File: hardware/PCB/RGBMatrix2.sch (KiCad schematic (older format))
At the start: 27 parts

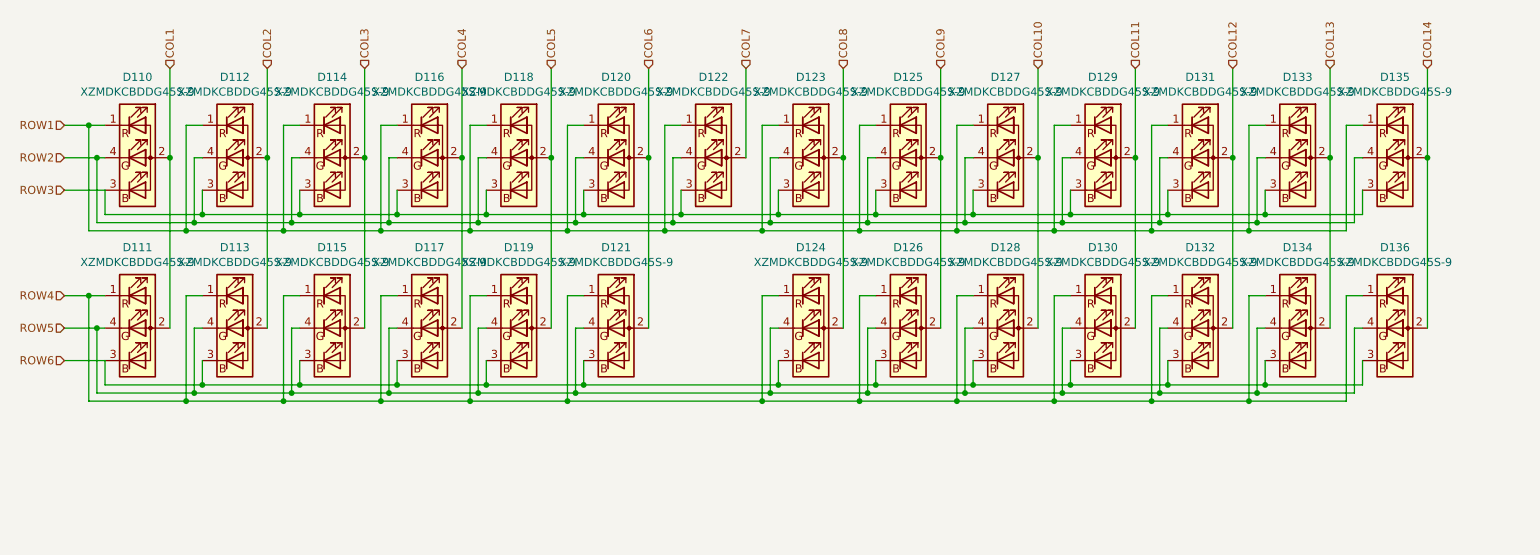
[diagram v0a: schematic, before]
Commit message: small improvements (cap distance)
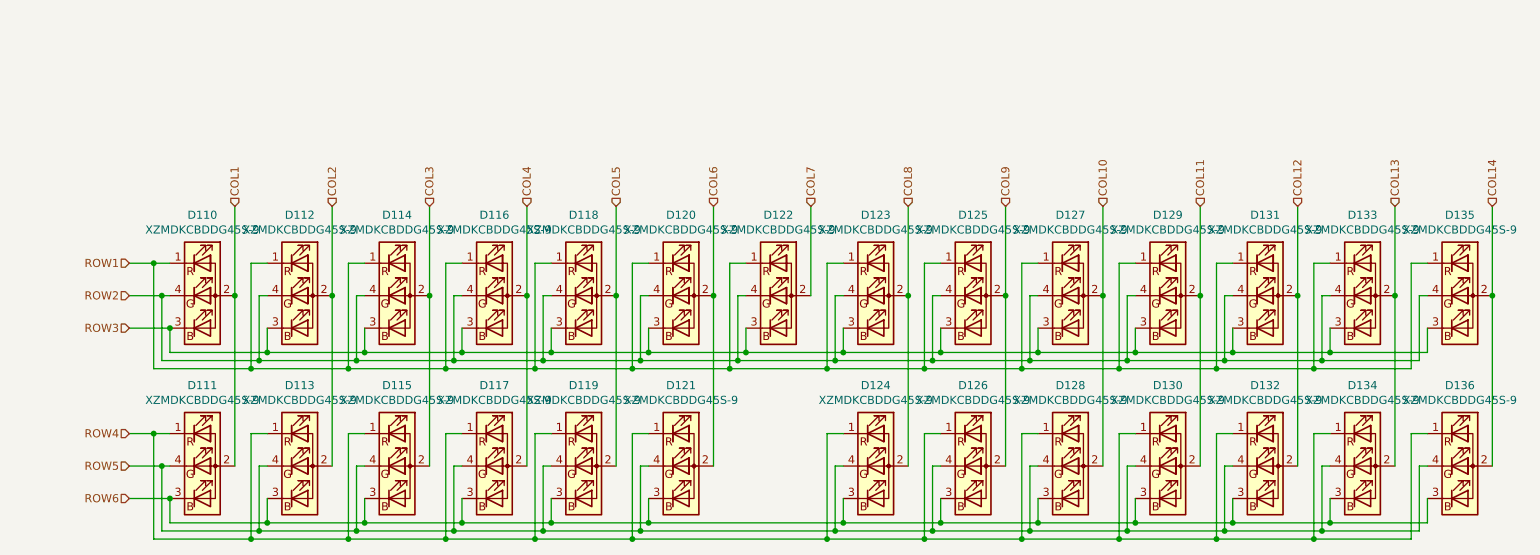
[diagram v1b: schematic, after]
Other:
- moved on the sheet: D110, D111, D112, D113, D114, D115, D116, D117, D118, D119, D120, D121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

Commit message: Make sure GPL done correctly, rev0.2 ready, not going to make it either
Need to make it nicer
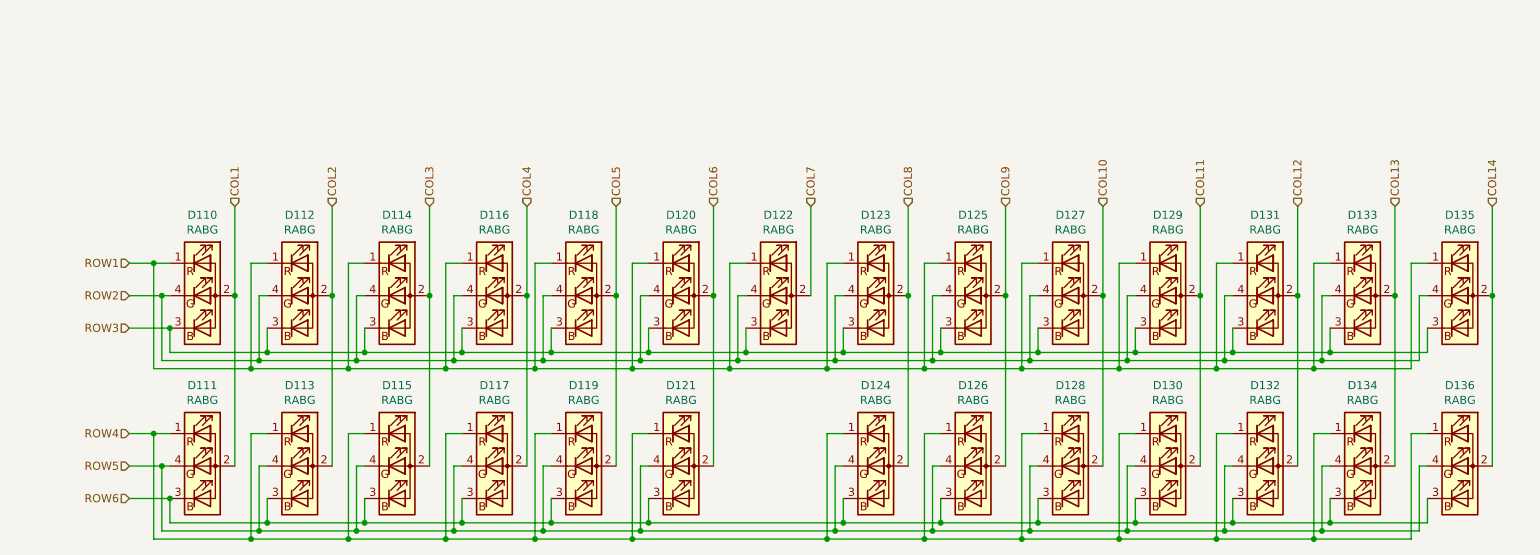
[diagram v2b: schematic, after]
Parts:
- D110, D111, D112, D113, D114, D115, D116, D117, D118, D119, D120, D121, D122, D123, D124, D125, D126, D127, D128, D129, D130, D131, D132, D133, D134, D135, D136: value XZMDKCBDDG45S-9 -> RABG
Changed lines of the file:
@@
 Sheet 5 6
 Title "NHW68"
-Date "2020-01-31"
-Rev "0.1"
+Date "2020-02-04"
+Rev "0.2"
 Comp ""
 Comment1 ""
@@
 AR Path="/5EC33E3D/5E12F961/5ECE6F4E" Ref="D110"  Part="1"
 F 0 "D110" H 2150 3747 50  0000 C CNN
-F 1 "XZMDKCBDDG45S-9" H 2150 3656 50  0000 C CNN
+F 1 "RABG" H 2150 3656 50  0000 C CNN
 F 2 "KiCad:XZMDKCBDDG45S9_fixed" H 2150 3200 50  0001 C CNN
 F 3 "https://www.sunledusa.com/products/spec/XZMDKCBDDG45S-9.pdf" H 2150 3200 50  0001 C CNN
@@
 AR Path="/5EC33E3D/5E12F961/5ECF7D8D" Ref="D112"  Part="1"
 F 0 "D112" H 2750 3747 50  0000 C CNN
-F 1 "XZMDKCBDDG45S-9" H 2750 3656 50  0000 C CNN
+F 1 "RABG" H 2750 3656 50  0000 C CNN
 F 2 "KiCad:XZMDKCBDDG45S9_fixed" H 2750 3200 50  0001 C CNN
 F 3 "https://www.sunledusa.com/products/spec/XZMDKCBDDG45S-9.pdf" H 2750 3200 50  0001 C CNN
@@
 AR Path="/5EC33E3D/5E12F961/5ED08C1C" Ref="D114"  Part="1"
 F 0 "D114" H 3350 3747 50  0000 C CNN
-F 1 "XZMDKCBDDG45S-9" H 3350 3656 50  0000 C CNN
+F 1 "RABG" H 3350 3656 50  0000 C CNN
 F 2 "KiCad:XZMDKCBDDG45S9_fixed" H 3350 3200 50  0001 C CNN
 F 3 "https://www.sunledusa.com/products/spec/XZMDKCBDDG45S-9.pdf" H 3350 3200 50  0001 C CNN
@@
 AR Path="/5EC33E3D/5E12F961/5ED19532" Ref="D116"  Part="1"
 F 0 "D116" H 3950 3747 50  0000 C CNN
-F 1 "XZMDKCBDDG45S-9" H 3950 3656 50  0000 C CNN
+F 1 "RABG" H 3950 3656 50  0000 C CNN
 F 2 "KiCad:XZMDKCBDDG45S9_fixed" H 3950 3200 50  0001 C CNN
 F 3 "https://www.sunledusa.com/products/spec/XZMDKCBDDG45S-9.pdf" H 3950 3200 50  0001 C CNN
@@
 AR Path="/5EC33E3D/5E12F961/5ED2A1D2" Ref="D118"  Part="1"
 F 0 "D118" H 4500 3747 50  0000 C CNN
-F 1 "XZMDKCBDDG45S-9" H 4500 3656 50  0000 C CNN
+F 1 "RABG" H 4500 3656 50  0000 C CNN
 F 2 "KiCad:XZMDKCBDDG45S9_fixed" H 4500 3200 50  0001 C CNN
 F 3 "https://www.sunledusa.com/products/spec/XZMDKCBDDG45S-9.pdf" H 4500 3200 50  0001 C CNN
@@
 AR Path="/5EC33E3D/5E12F961/5ED3AE35" Ref="D120"  Part="1"
 F 0 "D120" H 5100 3747 50  0000 C CNN
-F 1 "XZMDKCBDDG45S-9" H 5100 3656 50  0000 C CNN
+F 1 "RABG" H 5100 3656 50  0000 C CNN
 F 2 "KiCad:XZMDKCBDDG45S9_fixed" H 5100 3200 50  0001 C CNN
 F 3 "https://www.sunledusa.com/products/spec/XZMDKCBDDG45S-9.pdf" H 5100 3200 50  0001 C CNN
@@
 AR Path="/5EC33E3D/5E12F961/5ED4B8F9" Ref="D122"  Part="1"
 F 0 "D122" H 5700 3747 50  0000 C CNN
-F 1 "XZMDKCBDDG45S-9" H 5700 3656 50  0000 C CNN
+F 1 "RABG" H 5700 3656 50  0000 C CNN
 F 2 "KiCad:XZMDKCBDDG45S9_fixed" H 5700 3200 50  0001 C CNN
 F 3 "https://www.sunledusa.com/products/spec/XZMDKCBDDG45S-9.pdf" H 5700 3200 50  0001 C CNN
@@
 AR Path="/5EC33E3D/5E12F961/5ED5C37B" Ref="D123"  Part="1"
 F 0 "D123" H 6300 3747 50  0000 C CNN
-F 1 "XZMDKCBDDG45S-9" H 6300 3656 50  0000 C CNN
+F 1 "RABG" H 6300 3656 50  0000 C CNN
 F 2 "KiCad:XZMDKCBDDG45S9_fixed" H 6300 3200 50  0001 C CNN
 F 3 "https://www.sunledusa.com/products/spec/XZMDKCBDDG45S-9.pdf" H 6300 3200 50  0001 C CNN
@@
 AR Path="/5EC33E3D/5E12F961/5ED6CA4B" Ref="D125"  Part="1"
 F 0 "D125" H 6900 3747 50  0000 C CNN
-F 1 "XZMDKCBDDG45S-9" H 6900 3656 50  0000 C CNN
+F 1 "RABG" H 6900 3656 50  0000 C CNN
 F 2 "KiCad:XZMDKCBDDG45S9_fixed" H 6900 3200 50  0001 C CNN
 F 3 "https://www.sunledusa.com/products/spec/XZMDKCBDDG45S-9.pdf" H 6900 3200 50  0001 C CNN
@@
 AR Path="/5EC33E3D/5E12F961/5ED7D671" Ref="D127"  Part="1"
 F 0 "D127" H 7500 3747 50  0000 C CNN
-F 1 "XZMDKCBDDG45S-9" H 7500 3656 50  0000 C CNN
+F 1 "RABG" H 7500 3656 50  0000 C CNN
 F 2 "KiCad:XZMDKCBDDG45S9_fixed" H 7500 3200 50  0001 C CNN
 F 3 "https://www.sunledusa.com/products/spec/XZMDKCBDDG45S-9.pdf" H 7500 3200 50  0001 C CNN
@@
 AR Path="/5EC33E3D/5E12F961/5ED8E3BC" Ref="D129"  Part="1"
 F 0 "D129" H 8100 3747 50  0000 C CNN
-F 1 "XZMDKCBDDG45S-9" H 8100 3656 50  0000 C CNN
+F 1 "RABG" H 8100 3656 50  0000 C CNN
 F 2 "KiCad:XZMDKCBDDG45S9_fixed" H 8100 3200 50  0001 C CNN
 F 3 "https://www.sunledusa.com/products/spec/XZMDKCBDDG45S-9.pdf" H 8100 3200 50  0001 C CNN
@@
 AR Path="/5EC33E3D/5E12F961/5ED9EECC" Ref="D131"  Part="1"
 F 0 "D131" H 8700 3747 50  0000 C CNN
-F 1 "XZMDKCBDDG45S-9" H 8700 3656 50  0000 C CNN
+F 1 "RABG" H 8700 3656 50  0000 C CNN
 F 2 "KiCad:XZMDKCBDDG45S9_fixed" H 8700 3200 50  0001 C CNN
 F 3 "https://www.sunledusa.com/products/spec/XZMDKCBDDG45S-9.pdf" H 8700 3200 50  0001 C CNN
@@
 AR Path="/5EC33E3D/5E12F961/5EDAF8D0" Ref="D133"  Part="1"
 F 0 "D133" H 9300 3747 50  0000 C CNN
-F 1 "XZMDKCBDDG45S-9" H 9300 3656 50  0000 C CNN
+F 1 "RABG" H 9300 3656 50  0000 C CNN
 F 2 "KiCad:XZMDKCBDDG45S9_fixed" H 9300 3200 50  0001 C CNN
 F 3 "https://www.sunledusa.com/products/spec/XZMDKCBDDG45S-9.pdf" H 9300 3200 50  0001 C CNN
@@
 AR Path="/5EC33E3D/5E12F961/5EDC0468" Ref="D135"  Part="1"
 F 0 "D135" H 9900 3747 50  0000 C CNN
-F 1 "XZMDKCBDDG45S-9" H 9900 3656 50  0000 C CNN
+F 1 "RABG" H 9900 3656 50  0000 C CNN
 F 2 "KiCad:XZMDKCBDDG45S9_fixed" H 9900 3200 50  0001 C CNN
 F 3 "https://www.sunledusa.com/products/spec/XZMDKCBDDG45S-9.pdf" H 9900 3200 50  0001 C CNN
@@
 AR Path="/5EC33E3D/5E12F961/5EDF2634" Ref="D136"  Part="1"
 F 0 "D136" H 9900 4797 50  0000 C CNN
-F 1 "XZMDKCBDDG45S-9" H 9900 4706 50  0000 C CNN
+F 1 "RABG" H 9900 4706 50  0000 C CNN
 F 2 "KiCad:XZMDKCBDDG45S9_fixed" H 9900 4250 50  0001 C CNN
 F 3 "https://www.sunledusa.com/products/spec/XZMDKCBDDG45S-9.pdf" H 9900 4250 50  0001 C CNN
@@
 AR Path="/5EC33E3D/5E12F961/5EE13AA6" Ref="D132"  Part="1"
 F 0 "D132" H 8700 4797 50  0000 C CNN
-F 1 "XZMDKCBDDG45S-9" H 8700 4706 50  0000 C CNN
+F 1 "RABG" H 8700 4706 50  0000 C CNN
 F 2 "KiCad:XZMDKCBDDG45S9_fixed" H 8700 4250 50  0001 C CNN
 F 3 "https://www.sunledusa.com/products/spec/XZMDKCBDDG45S-9.pdf" H 8700 4250 50  0001 C CNN
@@
 AR Path="/5EC33E3D/5E12F961/5EE24547" Ref="D130"  Part="1"
 F 0 "D130" H 8100 4797 50  0000 C CNN
-F 1 "XZMDKCBDDG45S-9" H 8100 4706 50  0000 C CNN
+F 1 "RABG" H 8100 4706 50  0000 C CNN
 F 2 "KiCad:XZMDKCBDDG45S9_fixed" H 8100 4250 50  0001 C CNN
 F 3 "https://www.sunledusa.com/products/spec/XZMDKCBDDG45S-9.pdf" H 8100 4250 50  0001 C CNN
@@
 AR Path="/5EC33E3D/5E12F961/5EE34C17" Ref="D128"  Part="1"
 F 0 "D128" H 7500 4797 50  0000 C CNN
-F 1 "XZMDKCBDDG45S-9" H 7500 4706 50  0000 C CNN
+F 1 "RABG" H 7500 4706 50  0000 C CNN
 F 2 "KiCad:XZMDKCBDDG45S9_fixed" H 7500 4250 50  0001 C CNN
 F 3 "https://www.sunledusa.com/products/spec/XZMDKCBDDG45S-9.pdf" H 7500 4250 50  0001 C CNN
@@
 AR Path="/5EC33E3D/5E12F961/5EE45875" Ref="D126"  Part="1"
 F 0 "D126" H 6900 4797 50  0000 C CNN
-F 1 "XZMDKCBDDG45S-9" H 6900 4706 50  0000 C CNN
+F 1 "RABG" H 6900 4706 50  0000 C CNN
 F 2 "KiCad:XZMDKCBDDG45S9_fixed" H 6900 4250 50  0001 C CNN
 F 3 "https://www.sunledusa.com/products/spec/XZMDKCBDDG45S-9.pdf" H 6900 4250 50  0001 C CNN
@@
 AR Path="/5EC33E3D/5E12F961/5EE56B5B" Ref="D124"  Part="1"
 F 0 "D124" H 6300 4797 50  0000 C CNN
-F 1 "XZMDKCBDDG45S-9" H 6300 4706 50  0000 C CNN
+F 1 "RABG" H 6300 4706 50  0000 C CNN
 F 2 "KiCad:XZMDKCBDDG45S9_fixed" H 6300 4250 50  0001 C CNN
 F 3 "https://www.sunledusa.com/products/spec/XZMDKCBDDG45S-9.pdf" H 6300 4250 50  0001 C CNN
@@
 AR Path="/5EC33E3D/5E12F961/5EE68DA5" Ref="D121"  Part="1"
 F 0 "D121" H 5100 4797 50  0000 C CNN
-F 1 "XZMDKCBDDG45S-9" H 5100 4706 50  0000 C CNN
+F 1 "RABG" H 5100 4706 50  0000 C CNN
 F 2 "KiCad:XZMDKCBDDG45S9_fixed" H 5100 4250 50  0001 C CNN
 F 3 "https://www.sunledusa.com/products/spec/XZMDKCBDDG45S-9.pdf" H 5100 4250 50  0001 C CNN
@@
 AR Path="/5EC33E3D/5E12F961/5EE797FA" Ref="D119"  Part="1"
 F 0 "D119" H 4500 4797 50  0000 C CNN
-F 1 "XZMDKCBDDG45S-9" H 4500 4706 50  0000 C CNN
+F 1 "RABG" H 4500 4706 50  0000 C CNN
 F 2 "KiCad:XZMDKCBDDG45S9_fixed" H 4500 4250 50  0001 C CNN
 F 3 "https://www.sunledusa.com/products/spec/XZMDKCBDDG45S-9.pdf" H 4500 4250 50  0001 C CNN
@@
 AR Path="/5EC33E3D/5E12F961/5EE8A2F6" Ref="D117"  Part="1"
 F 0 "D117" H 3950 4797 50  0000 C CNN
-F 1 "XZMDKCBDDG45S-9" H 3950 4706 50  0000 C CNN
+F 1 "RABG" H 3950 4706 50  0000 C CNN
 F 2 "KiCad:XZMDKCBDDG45S9_fixed" H 3950 4250 50  0001 C CNN
 F 3 "https://www.sunledusa.com/products/spec/XZMDKCBDDG45S-9.pdf" H 3950 4250 50  0001 C CNN
@@
 AR Path="/5EC33E3D/5E12F961/5EEAC0EB" Ref="D115"  Part="1"
 F 0 "D115" H 3350 4797 50  0000 C CNN
-F 1 "XZMDKCBDDG45S-9" H 3350 4706 50  0000 C CNN
+F 1 "RABG" H 3350 4706 50  0000 C CNN
 F 2 "KiCad:XZMDKCBDDG45S9_fixed" H 3350 4250 50  0001 C CNN
 F 3 "https://www.sunledusa.com/products/spec/XZMDKCBDDG45S-9.pdf" H 3350 4250 50  0001 C CNN
@@
 AR Path="/5EC33E3D/5E12F961/5EEBC7BB" Ref="D113"  Part="1"
 F 0 "D113" H 2750 4797 50  0000 C CNN
-F 1 "XZMDKCBDDG45S-9" H 2750 4706 50  0000 C CNN
+F 1 "RABG" H 2750 4706 50  0000 C CNN
 F 2 "KiCad:XZMDKCBDDG45S9_fixed" H 2750 4250 50  0001 C CNN
 F 3 "https://www.sunledusa.com/products/spec/XZMDKCBDDG45S-9.pdf" H 2750 4250 50  0001 C CNN
@@
 AR Path="/5EC33E3D/5E12F961/5EECD5B2" Ref="D111"  Part="1"
 F 0 "D111" H 2150 4797 50  0000 C CNN
-F 1 "XZMDKCBDDG45S-9" H 2150 4706 50  0000 C CNN
+F 1 "RABG" H 2150 4706 50  0000 C CNN
 F 2 "KiCad:XZMDKCBDDG45S9_fixed" H 2150 4250 50  0001 C CNN
 F 3 "https://www.sunledusa.com/products/spec/XZMDKCBDDG45S-9.pdf" H 2150 4250 50  0001 C CNN
@@
 AR Path="/5EC33E3D/5E12F961/5EE030A2" Ref="D134"  Part="1"
 F 0 "D134" H 9300 4797 50  0000 C CNN
-F 1 "XZMDKCBDDG45S-9" H 9300 4706 50  0000 C CNN
+F 1 "RABG" H 9300 4706 50  0000 C CNN
 F 2 "KiCad:XZMDKCBDDG45S9_fixed" H 9300 4250 50  0001 C CNN
 F 3 "https://www.sunledusa.com/products/spec/XZMDKCBDDG45S-9.pdf" H 9300 4250 50  0001 C CNN

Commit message: Rev 0.5
1. Use a better 1205 LED (much chaper on LCSC)
2. Fix the crystal CL, Rext
3. did a better job on wiring (but might come with power issues?)
4. fix the key position (0.01mm shifted so its a big fix)
5. generate better bom files
6. add in LCSC and part number so easier to source
0.4 is gone
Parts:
- D110, D111, D112, D113, D114, D115, D116, D117, D118, D119, D120, D121, D122, D123, D124, D125, D126, D127, D128, D129, D130, D131, D132, D133, D134, D135, D136: footprint KiCad:XZMDKCBDDG45S9_fixed -> KiCad:RGB_LED_1205; LCSC (none) -> C409782; Part Number XZMDKCBDDG45S-9 -> MHT150RGBCT
